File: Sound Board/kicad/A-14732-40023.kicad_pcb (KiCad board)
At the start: 2 copper layers, 160 x 100.3 mm, 218 parts, among them P1 CONN_02X10, P5 VOLUME, P6 POWER, P7 SPEAKER, Q1 MPS3646, U1 OKI6295, U10 26LS32A, U11 26LS31, U12 27C040-100, U13 27C040-100, U14 YM2151, U15 TIL7524, U16 74ALS374, U17 74ALS174, U18 16L8-25, U19 74LS11, U2 2064, U20 74ALS139, U21 74LS14, U22 74LS74, U23 74LS74, U24 26LS31, U25 26LS32A, U26 74LS04, U28 YM3012, U29 LM324D, U3 27C040-100, U30 MC3340, U31 MB3731, U32 TL084D, U33 TL084D, U4 6809E, U5 74ALS374, U6 26LS32A, U7 26LS31, U8 74ALS138, U9 74LS74, Y1 3.5749MHz, Y2 8.0MHz

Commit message: New layout for larger board of 180x120mm
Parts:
- moved C12 242.9 mm to (26.0, 90.8)
- moved R89 240.2 mm to (26.0, 121.9)
- moved C32 234.2 mm to (47.0, 164.5)
- moved R34 233.0 mm to (39.4, 72.4)
- moved C47 222.3 mm to (34.3, 83.8)
- moved C99 220.4 mm to (26.0, 136.5)
- moved R32 213.9 mm to (34.3, 72.4)
- moved C49 210.3 mm to (39.4, 83.8)
- moved C13 209.3 mm to (47.0, 90.8)
- moved C103 208.7 mm to (26.0, 128.9)
- moved C15 208.0 mm to (67.9, 139.7)
- moved C16 194.1 mm to (86.4, 111.1)
- moved C26 192.1 mm to (50.2, 72.4)
- moved C14 190.5 mm to (67.9, 98.4)
- moved C2 186.9 mm to (66.0, 72.4)
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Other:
- board size 160 x 100.3 mm -> 180.3 x 120 mm

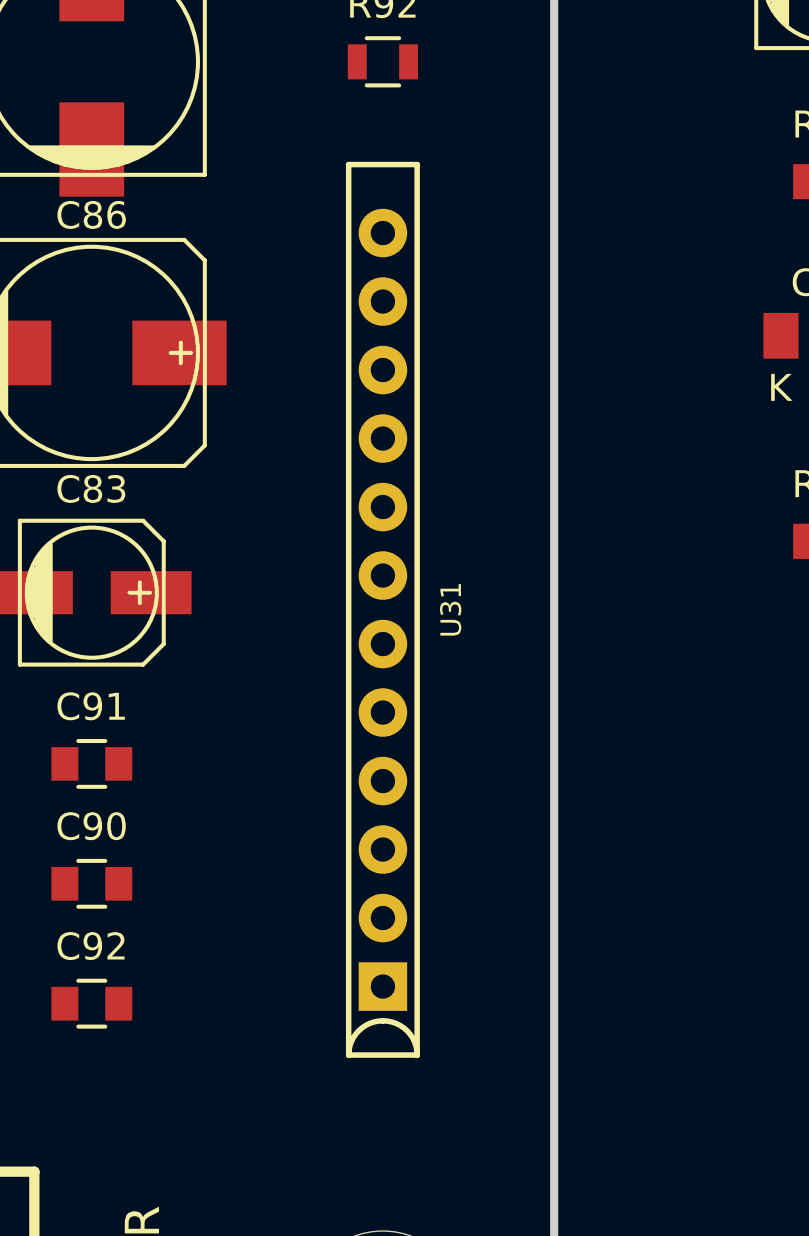
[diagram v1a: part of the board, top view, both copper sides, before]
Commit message: current layout for 180x120mm size
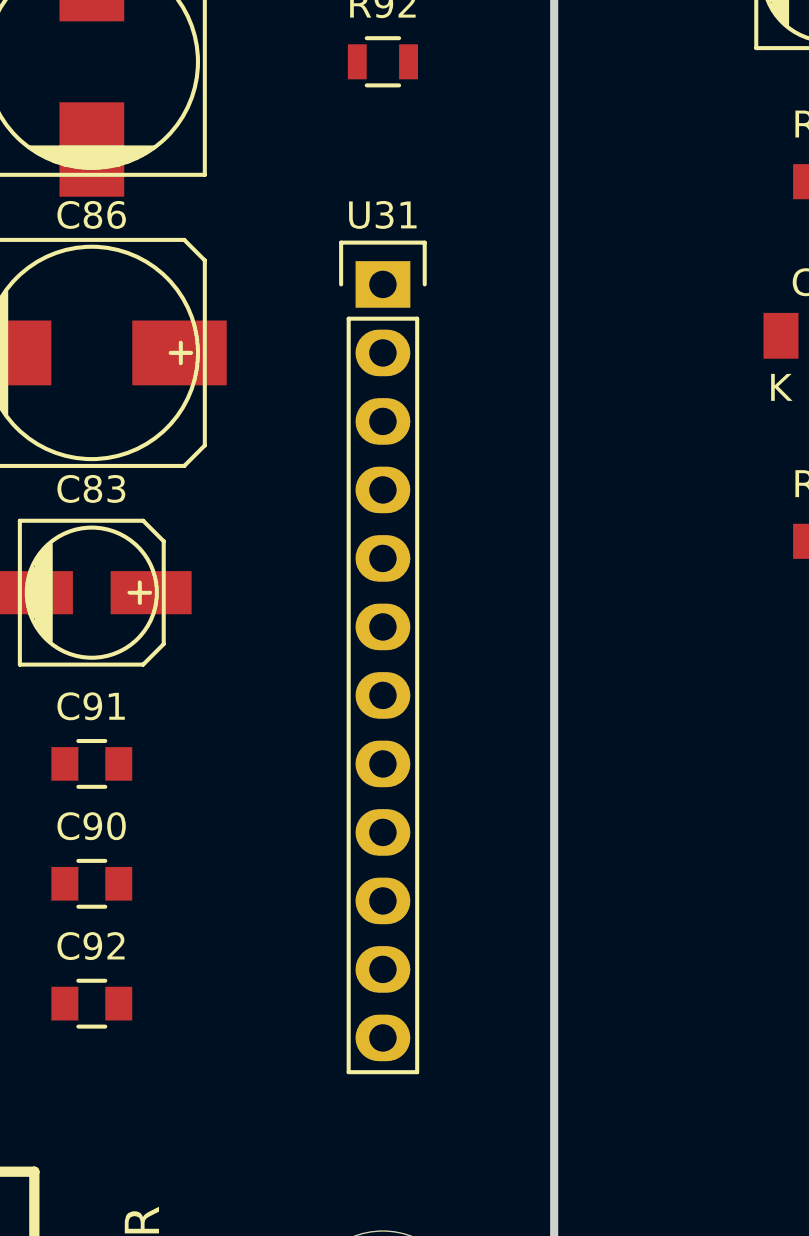
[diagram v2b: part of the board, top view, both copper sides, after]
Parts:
- U31: footprint A-14732-40023:SIP12 -> Pin_Headers:Pin_Header_Straight_1x12
- moved U31 12.1 mm to (188.0, 143.5), turned to 0 degrees
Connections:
- P1 pad 12: (no net) -> Net-(P1-Pad12)
- P1 pad 14: (no net) -> Net-(P1-Pad14)
- P1 pad 2: (no net) -> Net-(P1-Pad2)
- P1 pad 20: (no net) -> Net-(P1-Pad20)
- P5 pad 1: (no net) -> Net-(P5-Pad1)
- P5 pad 3: (no net) -> Net-(P5-Pad3)
- P6 pad 4: (no net) -> Net-(P6-Pad4)
- U1 pad 6: (no net) -> Net-(U1-Pad6)
- U11 pad 11: (no net) -> Net-(U11-Pad11)
- U11 pad 13: (no net) -> Net-(U11-Pad13)
- U11 pad 3: (no net) -> Net-(U11-Pad3)
- U11 pad 5: (no net) -> Net-(U11-Pad5)
- U15 pad 16: (no net) -> Net-(U15-Pad16)
- U16 pad 12: (no net) -> Net-(U16-Pad12)
- U16 pad 15: (no net) -> Net-(U16-Pad15)
- U16 pad 16: (no net) -> Net-(U16-Pad16)
- U16 pad 19: (no net) -> Net-(U16-Pad19)
- U18 pad 16: (no net) -> Net-(U18-Pad16)
- U20 pad 10: (no net) -> Net-(U20-Pad10)
- U20 pad 9: (no net) -> Net-(U20-Pad9)
- U22 pad 8: (no net) -> Net-(U22-Pad8)
- U22 pad 9: (no net) -> Net-(U22-Pad9)
- U23 pad 8: (no net) -> Net-(U23-Pad8)
- U24 pad 10: (no net) -> Net-(U24-Pad10)
- U24 pad 11: (no net) -> Net-(U24-Pad11)
- U24 pad 13: (no net) -> Net-(U24-Pad13)
- U24 pad 3: (no net) -> Net-(U24-Pad3)
- U24 pad 5: (no net) -> Net-(U24-Pad5)
- U31 pad 2: (no net) -> Net-(U31-Pad2)
- U4 pad 33: (no net) -> Net-(U4-Pad33)
- U4 pad 36: (no net) -> Net-(U4-Pad36)
- U4 pad 38: (no net) -> Net-(U4-Pad38)
- U4 pad 5: (no net) -> Net-(U4-Pad5)
- U4 pad 6: (no net) -> Net-(U4-Pad6)
- U7 pad 11: (no net) -> Net-(U7-Pad11)
- U7 pad 13: (no net) -> Net-(U7-Pad13)
- U7 pad 3: (no net) -> Net-(U7-Pad3)
- U7 pad 5: (no net) -> Net-(U7-Pad5)
- U8 pad 9: (no net) -> Net-(U8-Pad9)
- U9 pad 8: (no net) -> Net-(U9-Pad8)
- Y2 pad 1: (no net) -> Net-(Y2-Pad1)

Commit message: All components placed, time to play around
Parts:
- moved R48 264.7 mm to (19.1, 163.6), turned to 90 degrees
- moved C46 248.1 mm to (21.6, 157.0), turned to 270 degrees
- moved C61 246.0 mm to (36.3, 185.4), turned to 90 degrees
- moved C48 243.0 mm to (34.3, 160.0)
- moved R38 239.5 mm to (34.3, 163.8)
- moved R36 238.6 mm to (42.9, 170.9)
- moved C52 223.8 mm to (34.3, 170.9)
- moved R35 214.1 mm to (47.0, 156.2)
- moved R33 212.5 mm to (24.1, 163.6), turned to 270 degrees
- moved C60 209.2 mm to (71.6, 185.4), turned to 90 degrees
- moved R39 208.5 mm to (47.0, 165.1)
- moved R52 207.5 mm to (63.0, 185.4), turned to 90 degrees
- moved C58 206.6 mm to (47.0, 170.9)
- moved C51 204.1 mm to (40.8, 185.4), turned to 90 degrees
- moved C96 203.5 mm to (69.1, 172.7)
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
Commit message: fiddling around
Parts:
- moved C106 73.5 mm to (195.6, 118.1)
- moved R62 65.7 mm to (31.8, 158.1)
- moved C104 62.0 mm to (172.7, 71.6)
- moved C100 60.9 mm to (144.8, 129.5)
- moved C51 60.3 mm to (55.9, 127.0)
- moved C107 54.4 mm to (195.6, 113.0), turned to 0 degrees
- moved CR1 52.9 mm to (152.4, 129.5)
- moved R63 52.7 mm to (44.5, 158.1)
- moved C62 48.3 mm to (158.8, 128.0)
- moved R91 47.5 mm to (100.3, 134.6)
- moved R28 45.4 mm to (158.8, 132.1)
- moved C54 38.7 mm to (38.1, 178.4), turned to 0 degrees
- moved R52 38.3 mm to (31.8, 163.2), turned to 0 degrees
- moved C64 38.2 mm to (95.2, 146.1), turned to 270 degrees
- moved Q1 37.2 mm to (154.3, 128.9)
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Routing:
- added copper zone on B.Cu, net GND
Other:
- board size 180.3 x 120 mm -> 180.3 x 120.7 mm

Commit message: playing-laying
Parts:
- C10, C11, C12, C13, C14, C16, C17, C18, C19, C2, C20, C21, C22, C23, C24, C25, C26, C28, C29, C3, C32, C33, C4, C5, C6, C7, C8, C9: moved to B.Cu
- moved C40 131.6 mm to (176.5, 80.0), turned to 180 degrees
- moved C41 102.9 mm to (181.6, 82.5)
- moved C107 76.0 mm to (182.9, 38.1)
- moved C106 74.5 mm to (184.4, 44.5)
- moved C45 72.7 mm to (189.2, 39.4)
- moved R68 70.7 mm to (73.7, 121.9)
- moved C35 68.1 mm to (176.5, 61.0), turned to 180 degrees
- moved U16 67.3 mm to (125.7, 66.0)
- moved R69 66.9 mm to (62.2, 121.9)
- moved R29 66.2 mm to (123.2, 123.2)
- moved R23 66.1 mm to (125.7, 55.9), turned to 270 degrees
- moved R22 64.7 mm to (128.3, 55.9), turned to 270 degrees
- moved C44 63.3 mm to (168.9, 38.1)
- moved R30 63.2 mm to (123.2, 113.0)
- moved R25 62.4 mm to (130.8, 55.9), turned to 270 degrees
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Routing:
- net /Video Sound Generator Interface/SND_DAT6: track 0.00 -> 10.2 mm
- net /Video Sound Generator Interface/SND_DAT4: track 0.00 -> 9.71 mm
- net /Video Sound Generator Interface/SND_DAT7: track 0.00 -> 7.35 mm
- net /Video Sound Generator Interface/SND_DAT5: track 0.00 -> 7.35 mm
- added copper zone on F.Cu, net +12V
- added copper zone on F.Cu, net +5V
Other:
- board size 180.3 x 120.7 mm -> 180.3 x 139.7 mm
- net class Default: clearance 0.2 -> 0.15
- rule trace_clearance: 0.2 -> 0.15

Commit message: playing around
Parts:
- C104, C105, C106, C107, C35, C36, C37, C38, C39, C40, C41, C42, C43, C44, C45: moved to B.Cu
- moved C104 67.3 mm to (188.0, 95.2), turned to 270 degrees
- moved C107 57.1 mm to (182.9, 95.2), turned to 90 degrees
- moved C105 56.8 mm to (185.4, 95.2), turned to 270 degrees
- moved C45 51.6 mm to (180.3, 90.2)
- moved C106 51.0 mm to (180.3, 95.2), turned to 270 degrees
- moved C44 50.8 mm to (180.3, 87.6)
- moved R91 44.9 mm to (87.6, 77.5)
- moved C18 44.9 mm to (87.6, 95.2)
- moved U18 44.9 mm to (87.6, 95.2)
- moved C43 43.9 mm to (180.3, 85.1)
- moved R27 39.8 mm to (124.5, 101.6), turned to 180 degrees
- moved C16 38.1 mm to (87.6, 67.3)
- moved U16 38.1 mm to (87.6, 67.3)
- moved R22 38.1 mm to (90.2, 55.9)
- moved R23 38.1 mm to (87.6, 55.9)
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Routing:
- net /Video Sound Generator Interface/SND_DAT6: track 10.2 -> 0.00 mm
- net /Video Sound Generator Interface/SND_DAT4: track 9.71 -> 0.00 mm
- net /Video Sound Generator Interface/SND_DAT7: track 7.35 -> 0.00 mm
- net /Video Sound Generator Interface/SND_DAT5: track 7.35 -> 0.00 mm
